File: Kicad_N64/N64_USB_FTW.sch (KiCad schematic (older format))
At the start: 28 parts, among them IC1 ATMEGA8-AI, P1 CONN_3X2, P2 CONN_4X2, U1 LM317, X1 12mhz, X2 USB-MB-S

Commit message: added approximated power consumption, started pcb layout, finished some of wireless module schematic
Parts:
- removed R10, R6, R9: 0, symbol R
- added C1, C16, C6: 100n, symbol C
- added N1: CONN_3, symbol CONN_3
- R5: value 0 -> 10k
- renumbered C6 to C14, C1 to C14a1
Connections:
- net GND: now also R5.1, C1.2, C16.2, C6.2
- net MCU_VCC: now also C5.1, IC1.4 (VCC), IC1.6 (VCC), P1.2, R4.2, R7.1, U1.3 (OUT), C6.1, N1.2 (PM); no longer R5.2
- net VCC: now also C1.1, C16.1; no longer IC1.4 (VCC), IC1.6 (VCC), P1.2, P2.2, R5.1
- net WirelessVcc: now reaches IC1.23 ((ADC0)PC0)
- net WirelessVcc: now also P2.2, R5.2, N1.3 (P3)
- net at D1.2 (K), X2.D-: now also R1.2, R3.1
- net From regulator renamed ControllerVcc
- net ControllerVcc: now also N1.1 (P1); no longer R4.2
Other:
- moved on the sheet: P2

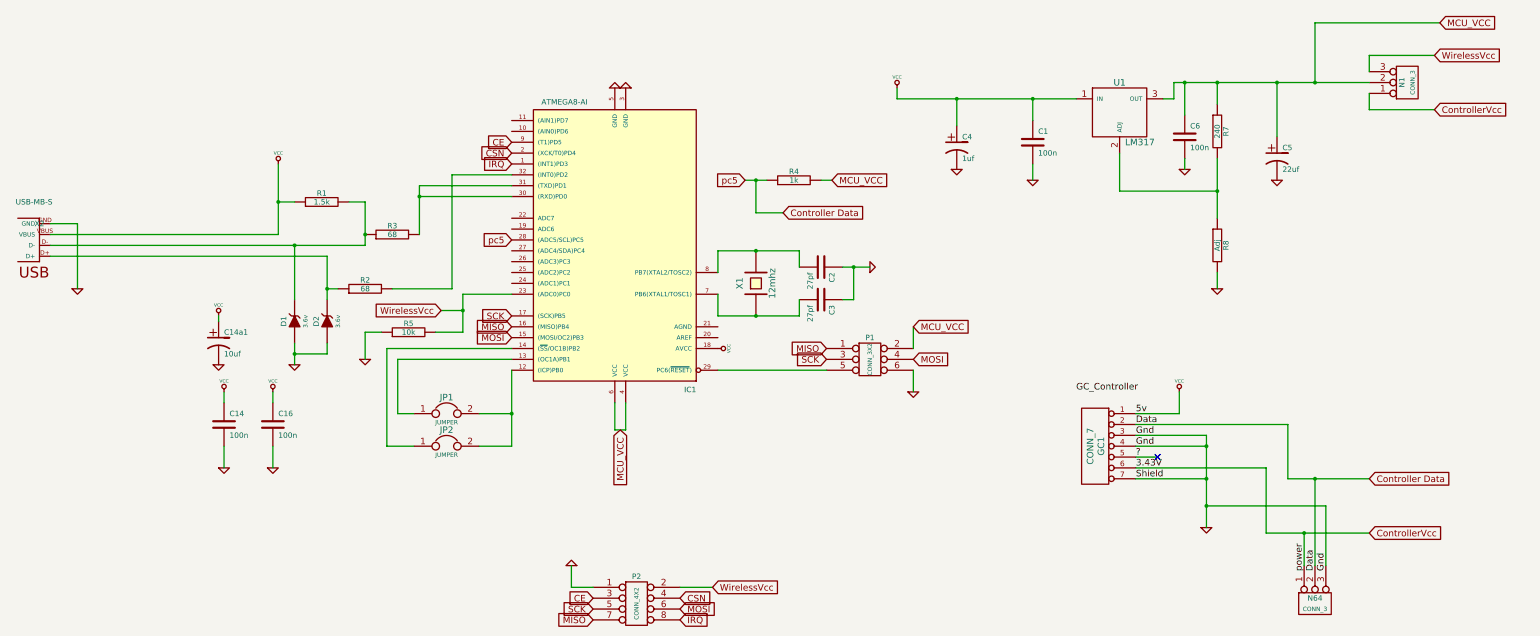
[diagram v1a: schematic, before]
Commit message: errors in schematic, wrong number of connectors for nfr. removed switch for wireless and nonwireless power. started making board layout
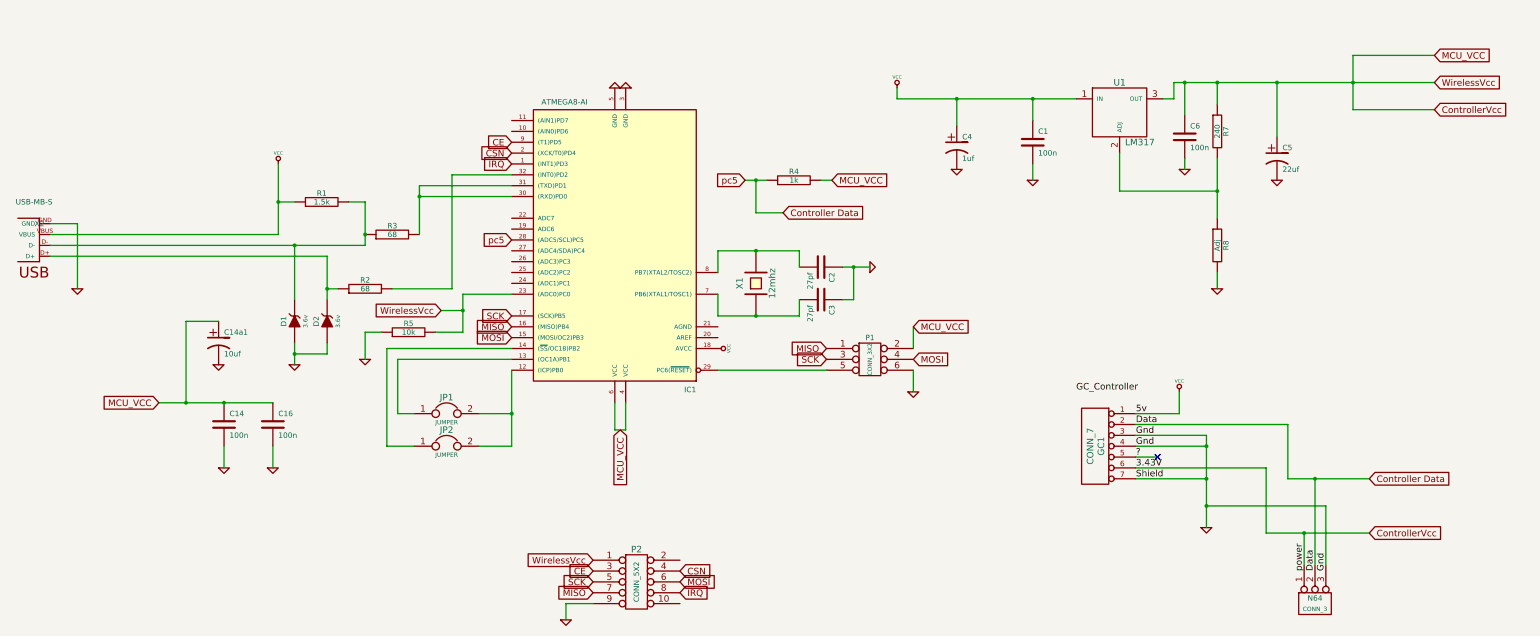
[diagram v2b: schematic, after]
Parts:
- removed N1: CONN_3, symbol CONN_3
- removed P2: CONN_4X2, symbol CONN_4X2
- added P2: CONN_5X2, symbol CONN_5X2
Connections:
- net MCU_VCC is gone; now on net ControllerVcc: C5.1, C6.1, IC1.4 (VCC), IC1.6 (VCC), P1.2, R4.2, R7.1, U1.3 (OUT)
- net WirelessVcc is gone; now on net ControllerVcc: IC1.23 ((ADC0)PC0), R5.2
- net CE: now also P2.3
- net CSN: now also P2.4
- net ControllerVcc: now also C14.1, C14a1.1, C16.1, P2.1
- net GND: now also P2.9
- net IRQ: now also P2.8
- net MISO: now also P2.7
- net MOSI: now also P2.6
- net SCK: now also P2.5
- net VCC: no longer C14.1, C14a1.1, C16.1

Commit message: fiddled a bit with some routing
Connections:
- net ControllerVcc: now also IC1.18 (AVCC)
- net VCC: no longer IC1.18 (AVCC)
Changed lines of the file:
@@
-EESchema Schematic File Version 2  date Tue 20 Mar 2012 11:08:43 PM CET
+EESchema Schematic File Version 2  date 09-05-2012 21:22:02
 LIBS:power
 LIBS:device
@@
 Sheet 1 1
 Title ""
-Date "20 mar 2012"
+Date "9 may 2012"
 Rev ""
 Comp ""
@@
 $EndDescr
 Wire Wire Line
+	7800 4600 7700 4600
+Wire Wire Line
+	14300 2150 11900 2150
+Wire Wire Line
+	13550 2400 13550 1900
+Wire Wire Line
+	13550 2400 14300 2400
+Connection ~ 2800 5100
+Wire Wire Line
+	2800 5100 2800 4350
+Wire Wire Line
+	2800 4350 3100 4350
+Wire Wire Line
+	1550 3650 4450 3650
+Wire Wire Line
+	1550 3450 1800 3450
+Wire Wire Line
+	12000 2950 12000 2850
+Connection ~ 12000 2150
+Connection ~ 10600 2300
+Wire Wire Line
+	10600 2500 10600 2300
+Wire Wire Line
+	4450 4700 4450 4450
+Wire Wire Line
+	4450 4450 4600 4450
+Wire Wire Line
+	8650 3050 8750 3050
+Wire Wire Line
+	6850 5350 6750 5350
+Wire Wire Line
+	6850 5350 6850 5100
+Connection ~ 3800 3650
+Wire Wire Line
+	4450 3650 4450 3250
+Wire Wire Line
+	3150 5500 3150 5700
+Wire Wire Line
+	12300 3900 12300 4050
+Wire Wire Line
+	11800 2300 11900 2300
+Wire Wire Line
+	11900 2300 11900 2150
+Connection ~ 12200 6050
+Wire Wire Line
+	12200 6050 13300 6050
+Wire Wire Line
+	13300 6050 13300 6600
+Connection ~ 13100 6300
+Wire Wire Line
+	13100 6600 13100 6300
+Connection ~ 12200 5500
+Wire Wire Line
+	11550 5500 12200 5500
+Wire Wire Line
+	12750 5700 12750 6300
+Wire Wire Line
+	12750 5700 11550 5700
+Wire Wire Line
+	11950 5000 11950 5200
+Wire Wire Line
+	11950 5200 11550 5200
+Wire Wire Line
+	12850 2150 12850 2650
+Connection ~ 12850 2150
+Wire Wire Line
+	12300 2150 12300 2350
+Wire Wire Line
+	12300 3150 11400 3150
+Wire Wire Line
+	9900 2300 9900 2550
+Wire Wire Line
+	4750 5200 4750 4700
+Wire Wire Line
+	4750 5200 4900 5200
+Wire Wire Line
+	4750 4700 5800 4700
+Wire Wire Line
+	5500 5500 5800 5500
+Wire Wire Line
+	5800 5500 5800 4800
+Connection ~ 8050 4300
+Wire Wire Line
+	7700 4300 8450 4300
+Connection ~ 8050 3700
+Wire Wire Line
+	8450 3850 8450 3700
+Wire Wire Line
+	8450 3700 7700 3700
+Connection ~ 8950 3850
+Wire Wire Line
+	8950 3850 8950 4150
+Wire Wire Line
+	8950 4150 8850 4150
+Wire Wire Line
+	8300 3350 8050 3350
+Connection ~ 8050 3050
+Wire Wire Line
+	8050 3350 8050 3050
+Wire Wire Line
+	4950 3550 4950 3100
+Wire Wire Line
+	4950 3100 5800 3100
+Wire Wire Line
+	4200 4050 4100 4050
+Connection ~ 4100 4050
+Wire Wire Line
+	3650 2900 3650 3550
+Wire Wire Line
+	4450 3250 4300 3250
+Connection ~ 4450 3550
+Wire Wire Line
+	3800 4150 3800 3650
+Wire Wire Line
+	3800 4650 4100 4650
+Wire Wire Line
+	4100 4650 4100 4550
+Connection ~ 3800 4650
+Wire Wire Line
+	4100 4150 4100 3750
+Wire Wire Line
+	3800 4750 3800 4550
+Wire Wire Line
+	4700 4050 5250 4050
+Wire Wire Line
+	5250 4050 5250 3000
+Wire Wire Line
+	5250 3000 5800 3000
+Wire Wire Line
+	5800 3200 4950 3200
+Connection ~ 4950 3200
+Wire Wire Line
+	9500 4800 9500 5000
+Wire Wire Line
+	7950 3050 8150 3050
+Wire Wire Line
+	7700 4800 8700 4800
+Wire Wire Line
+	9100 3850 8850 3850
+Wire Wire Line
+	7700 3700 7700 3900
+Wire Wire Line
+	7700 4300 7700 4100
+Wire Wire Line
+	8450 4300 8450 4150
+Wire Wire Line
+	5500 5200 5800 5200
+Connection ~ 5800 5200
+Wire Wire Line
+	4900 5500 4650 5500
+Wire Wire Line
+	4650 5500 4650 4600
+Wire Wire Line
+	4650 4600 5800 4600
+Connection ~ 9900 2300
+Wire Wire Line
+	12300 3400 12300 2850
+Connection ~ 12300 3150
+Connection ~ 12300 2150
+Wire Wire Line
+	11550 5600 11750 5600
+Wire Wire Line
+	11550 5300 12950 5300
+Wire Wire Line
+	12950 5300 12950 5800
+Wire Wire Line
+	12950 5800 13700 5800
+Wire Wire Line
+	11550 5400 12200 5400
+Wire Wire Line
+	12200 5400 12200 6250
+Wire Wire Line
+	12200 5800 11550 5800
+Connection ~ 12200 5800
+Wire Wire Line
+	13200 6600 13200 5800
+Connection ~ 13200 5800
+Wire Wire Line
+	3800 3250 3650 3250
+Connection ~ 3650 3250
+Wire Wire Line
+	11000 2300 9350 2300
+Wire Wire Line
+	11400 3150 11400 2800
+Wire Wire Line
+	1800 3450 1800 4050
+Wire Wire Line
+	6750 5350 6750 5100
+Wire Wire Line
+	9500 4400 9500 4600
+Wire Wire Line
+	9350 2300 9350 2200
+Wire Wire Line
+	3600 5500 3600 5700
+Wire Wire Line
+	12750 6300 13700 6300
+Wire Wire Line
+	5150 4250 5350 4250
+Wire Wire Line
+	5800 4100 5350 4100
+Wire Wire Line
+	5100 4450 5350 4450
+Wire Wire Line
+	5350 4450 5350 4100
+Connection ~ 5350 4250
+Wire Wire Line
+	10600 2900 10600 3050
+Wire Wire Line
+	12000 2450 12000 2150
+Wire Wire Line
+	3650 3550 1550 3550
+Wire Wire Line
+	4100 3750 1550 3750
+Wire Wire Line
+	2550 5100 3600 5100
+Connection ~ 3150 5100
+Wire Wire Line
+	6550 6950 6300 6950
+Wire Wire Line
+	6300 6950 6300 7100
+Connection ~ 13550 2150
+Wire Wire Line
 	13550 1900 14300 1900
-Connection ~ 13550 2150
-Wire Wire Line
-	6300 7100 6300 6950
-Wire Wire Line
-	6300 6950 6550 6950
-Connection ~ 3150 5100
-Wire Wire Line
-	2550 5100 3600 5100
-Wire Wire Line
-	4100 3750 1550 3750
-Wire Wire Line
-	3650 3550 1550 3550
-Wire Wire Line
-	12000 2450 12000 2150
-Wire Wire Line
-	10600 2900 10600 3050
-Connection ~ 5350 4250
-Wire Wire Line
-	5350 4450 5350 4100
-Wire Wire Line
-	5350 4450 5100 4450
-Wire Wire Line
-	5350 4100 5800 4100
-Wire Wire Line
-	5150 4250 5350 4250
-Wire Wire Line
-	13700 6300 12750 6300
-Wire Wire Line
-	3600 5500 3600 5700
-Wire Wire Line
-	9350 2300 9350 2200
-Wire Wire Line
-	9500 4400 9500 4600
-Wire Wire Line
-	6750 5100 6750 5350
-Wire Wire Line
-	1800 4050 1800 3450
-Wire Wire Line
-	11400 2800 11400 3150
-Wire Wire Line
-	11000 2300 9350 2300
-Connection ~ 3650 3250
-Wire Wire Line
-	3800 3250 3650 3250
-Connection ~ 13200 5800
-Wire Wire Line
-	13200 6600 13200 5800
-Connection ~ 12200 5800
-Wire Wire Line
-	12200 5800 11550 5800
-Wire Wire Line
-	12200 6250 12200 5400
-Wire Wire Line
-	12200 5400 11550 5400
-Wire Wire Line
-	13700 5800 12950 5800
-Wire Wire Line
-	12950 5800 12950 5300
-Wire Wire Line
-	12950 5300 11550 5300
-Wire Wire Line
-	11550 5600 11750 5600
-Connection ~ 12300 2150
-Connection ~ 12300 3150
-Wire Wire Line
-	12300 3400 12300 2850
-Connection ~ 9900 2300
-Wire Wire Line
-	5800 4600 4650 4600
-Wire Wire Line
-	4650 4600 4650 5500
-Wire Wire Line
-	4650 5500 4900 5500
-Connection ~ 5800 5200
-Wire Wire Line
-	5500 5200 5800 5200
-Wire Wire Line
-	8450 4300 8450 4150
-Wire Wire Line
-	7700 4300 7700 4100
-Wire Wire Line
-	7700 3700 7700 3900
-Wire Wire Line
-	9100 3850 8850 3850
-Wire Wire Line
-	7700 4800 8700 4800
-Wire Wire Line
-	7950 3050 8150 3050
-Wire Wire Line
-	9500 4800 9500 5000
-Connection ~ 4950 3200
-Wire Wire Line
-	5800 3200 4950 3200
-Wire Wire Line
-	5800 3000 5250 3000
-Wire Wire Line
-	5250 3000 5250 4050
-Wire Wire Line
-	5250 4050 4700 4050
-Wire Wire Line
-	3800 4750 3800 4550
-Wire Wire Line
-	4100 4150 4100 3750
-Connection ~ 3800 4650
-Wire Wire Line
-	4100 4550 4100 4650
-Wire Wire Line
-	4100 4650 3800 4650
-Wire Wire Line
-	3800 4150 3800 3650
-Connection ~ 4450 3550
-Wire Wire Line
-	4450 3250 4300 3250
-Wire Wire Line
-	3650 2900 3650 3550
-Connection ~ 4100 4050
-Wire Wire Line
-	4200 4050 4100 4050
-Wire Wire Line
-	4950 3100 5800 3100
-Wire Wire Line
-	4950 3550 4950 3100
-Wire Wire Line
-	8050 3050 8050 3350
-Connection ~ 8050 3050
-Wire Wire Line
-	8050 3350 8300 3350
-Wire Wire Line
-	8850 4150 8950 4150
-Wire Wire Line
-	8950 4150 8950 3850
-Connection ~ 8950 3850
-Wire Wire Line
-	7700 3700 8450 3700
-Wire Wire Line
-	8450 3700 8450 3850
-Connection ~ 8050 3700
-Wire Wire Line
-	8450 4300 7700 4300
-Connection ~ 8050 4300
-Wire Wire Line
-	5800 4800 5800 5500
-Wire Wire Line
-	5800 5500 5500 5500
-Wire Wire Line
-	5800 4700 4750 4700
-Wire Wire Line
-	4900 5200 4750 5200
-Wire Wire Line
-	4750 5200 4750 4700
-Wire Wire Line
-	9900 2300 9900 2550
-Wire Wire Line
-	11400 3150 12300 3150
-Wire Wire Line
-	12300 2150 12300 2350
-Connection ~ 12850 2150
-Wire Wire Line
-	12850 2150 12850 2650
-Wire Wire Line
-	11550 5200 11950 5200
-Wire Wire Line
-	11950 5200 11950 5000
-Wire Wire Line
-	11550 5700 12750 5700
-Wire Wire Line
-	12750 5700 12750 6300
-Wire Wire Line
-	11550 5500 12200 5500
-Connection ~ 12200 5500
-Wire Wire Line
-	13100 6600 13100 6300
-Connection ~ 13100 6300
-Wire Wire Line
-	13300 6600 13300 6050
-Wire Wire Line
-	13300 6050 12200 6050
-Connection ~ 12200 6050
-Wire Wire Line
-	11900 2150 11900 2300
-Wire Wire Line
-	11900 2300 11800 2300
-Wire Wire Line
-	12300 3900 12300 4050
-Wire Wire Line
-	3150 5500 3150 5700
-Wire Wire Line
-	4450 3650 4450 3250
-Connection ~ 3800 3650
-Wire Wire Line
-	6850 5100 6850 5350
-Wire Wire Line
-	6850 5350 6750 5350
-Wire Wire Line
-	8650 3050 8750 3050
-Wire Wire Line
-	4600 4450 4450 4450
-Wire Wire Line
-	4450 4450 4450 4700
-Wire Wire Line
-	10600 2500 10600 2300
-Connection ~ 10600 2300
-Connection ~ 12000 2150
-Wire Wire Line
-	12000 2950 12000 2850
-Wire Wire Line
-	1800 3450 1550 3450
-Wire Wire Line
-	1550 3650 4450 3650
-Wire Wire Line
-	3100 4350 2800 4350
-Wire Wire Line
-	2800 4350 2800 5100
-Connection ~ 2800 5100
-Wire Wire Line
-	13550 2400 14300 2400
-Wire Wire Line
-	13550 1900 13550 2400
-Wire Wire Line
-	14300 2150 11900 2150
+Text GLabel 7800 4600 2    60   Input ~ 0
+MCU_VCC
 $Comp
 L CONN_5X2 P2
@@
 	0    1    1    0
 $EndComp
-$Comp
-L VCC #PWR015
-U 1 1 4F43FE9B
-P 7700 4600
-F 0 "#PWR015" H 7700 4700 30  0001 C CNN
-F 1 "VCC" H 7700 4700 30  0000 C CNN
-	1    7700 4600
-	0    1    1    0
-$EndComp
